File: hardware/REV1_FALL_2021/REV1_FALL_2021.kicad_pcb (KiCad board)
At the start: 2 copper layers, 146 x 133.4 mm, 24 parts, among them J101 Screw_Terminal_01x02, Q101 Q_NMOS_GDS, U1 Teensy3.6_All_Pins, U2 PA16165_Breakout, U201 TPS2113ADRBR, U3 MPL3115A2_Breakout, U301 TPS2113ADRBR, U4 BNO055_Breakout, U5 RFM69HCW_Breakout

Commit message: finish layout
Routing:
- net /BALANCE_CONTROL: track 0.00 -> 55.8 mm, vias 0 -> 1
- net GND: track 157.8 -> 213.3 mm, vias 6 -> 23
- net /TPS_1_STAT: track 3.41 -> 54.9 mm, vias 0 -> 1
- net /TPS_2_STAT: track 4.27 -> 50.5 mm, vias 0 -> 1
- net /V_TEENSY: track 113.5 -> 117.8 mm
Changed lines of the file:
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@@
     (thickness 1.6)
     (drawings 5)
-    (tracks 213)
+    (tracks 275)
     (zones 0)
     (modules 24)
@@
   )
   (setup
-    (last_trace_width 0.762)
+    (last_trace_width 0.25)
     (user_trace_width 0.4318)
     (user_trace_width 0.762)
@@
   (segment (start 104.832998 116.274002) (end 104.832998 120.211002) (width 0.25) (layer B.Cu) (net 11))
   (segment (start 104.832998 116.274002) (end 108.331 112.776) (width 0.25) (layer B.Cu) (net 11))
+  (segment (start 38.0365 88.35) (end 37.126 88.35) (width 0.25) (layer F.Cu) (net 12) (status 400000))
+  (via (at 54.864 89.408) (size 1.016) (drill 0.635) (layers F.Cu B.Cu) (net 12))
+  (segment (start 52.832 91.44) (end 54.864 89.408) (width 0.25) (layer F.Cu) (net 12))
+  (via (at 52.832 91.44) (size 1.016) (drill 0.635) (layers F.Cu B.Cu) (net 12))
+  (segment (start 49.784 91.44) (end 52.832 91.44) (width 0.25) (layer B.Cu) (net 12))
+  (via (at 49.784 91.44) (size 1.016) (drill 0.635) (layers F.Cu B.Cu) (net 12))
+  (segment (start 43.18 91.44) (end 49.784 91.44) (width 0.25) (layer F.Cu) (net 12))
+  (via (at 43.18 91.44) (size 1.016) (drill 0.635) (layers F.Cu B.Cu) (net 12))
+  (segment (start 40.132 91.44) (end 43.18 91.44) (width 0.25) (layer B.Cu) (net 12))
+  (via (at 40.132 91.44) (size 1.016) (drill 0.635) (layers F.Cu B.Cu) (net 12))
+  (segment (start 37.084 91.44) (end 40.132 91.44) (width 0.25) (layer F.Cu) (net 12))
+  (via (at 37.084 91.44) (size 1.016) (drill 0.635) (layers F.Cu B.Cu) (net 12))
+  (segment (start 34.036 91.44) (end 37.084 91.44) (width 0.25) (layer B.Cu) (net 12))
+  (via (at 34.036 91.44) (size 1.016) (drill 0.635) (layers F.Cu B.Cu) (net 12))
+  (segment (start 37.126 88.35) (end 34.036 91.44) (width 0.25) (layer F.Cu) (net 12))
+  (segment (start 42.7765 82.9975) (end 41.4625 82.9975) (width 0.25) (layer F.Cu) (net 12) (status 400000))
+  (via (at 39.624 78.74) (size 1.016) (drill 0.635) (layers F.Cu B.Cu) (net 12))
+  (segment (start 39.624 80.772) (end 39.624 78.74) (width 0.25) (layer F.Cu) (net 12))
+  (segment (start 40.132 81.28) (end 39.624 80.772) (width 0.25) (layer F.Cu) (net 12))
+  (via (at 40.132 81.28) (size 1.016) (drill 0.635) (layers F.Cu B.Cu) (net 12))
+  (segment (start 40.132 84.328) (end 40.132 81.28) (width 0.25) (layer B.Cu) (net 12))
+  (via (at 40.132 84.328) (size 1.016) (drill 0.635) (layers F.Cu B.Cu) (net 12))
+  (segment (start 41.4625 82.9975) (end 40.132 84.328) (width 0.25) (layer F.Cu) (net 12))
+  (segment (start 44.0765 80.1975) (end 44.0765 79.3675) (width 0.25) (layer F.Cu) (net 12) (status 400000))
+  (via (at 53.848 84.836) (size 1.016) (drill 0.635) (layers F.Cu B.Cu) (net 12))
+  (segment (start 54.864 84.836) (end 53.848 84.836) (width 0.25) (layer B.Cu) (net 12))
+  (segment (start 55.88 83.82) (end 54.864 84.836) (width 0.25) (layer B.Cu) (net 12))
+  (via (at 55.88 83.82) (size 1.016) (drill 0.635) (layers F.Cu B.Cu) (net 12))
+  (segment (start 55.88 80.264) (end 55.88 83.82) (width 0.25) (layer F.Cu) (net 12))
+  (segment (start 44.0765 79.3675) (end 44.704 78.74) (width 0.25) (layer F.Cu) (net 12))
+  (segment (start 44.704 78.74) (end 45.212 78.74) (width 0.25) (layer F.Cu) (net 12))
+  (via (at 45.212 78.74) (size 1.016) (drill 0.635) (layers F.Cu B.Cu) (net 12))
+  (segment (start 45.212 78.74) (end 48.26 78.74) (width 0.25) (layer B.Cu) (net 12))
+  (via (at 48.26 78.74) (size 1.016) (drill 0.635) (layers F.Cu B.Cu) (net 12))
+  (segment (start 48.26 78.74) (end 51.308 78.74) (width 0.25) (layer F.Cu) (net 12))
+  (via (at 51.308 78.74) (size 1.016) (drill 0.635) (layers F.Cu B.Cu) (net 12))
+  (segment (start 51.308 78.74) (end 54.356 78.74) (width 0.25) (layer B.Cu) (net 12))
+  (via (at 54.356 78.74) (size 1.016) (drill 0.635) (layers F.Cu B.Cu) (net 12))
+  (segment (start 54.356 78.74) (end 55.88 80.264) (width 0.25) (layer F.Cu) (net 12))
+  (via (at 55.88 80.264) (size 1.016) (drill 0.635) (layers F.Cu B.Cu) (net 12))
   (segment (start 41.473 98.555) (end 41.473 101.854) (width 0.4318) (layer F.Cu) (net 13) (status 400000))
   (segment (start 41.473 101.854) (end 41.473 102.1575) (width 0.4318) (layer F.Cu) (net 13) (status 800000))
@@
   (via (at 46.6725 88.0745) (size 0.8) (drill 0.4) (layers F.Cu B.Cu) (net 14))
   (segment (start 44.873 86.275) (end 46.6725 88.0745) (width 0.4318) (layer F.Cu) (net 14) (status 400000))
-  (segment (start 88.265 157.099) (end 70.739 157.099) (width 0.762) (layer B.Cu) (net 14) (status 400000))
-  (segment (start 60.071 98.425) (end 49.7205 88.0745) (width 0.762) (layer B.Cu) (net 14))
-  (segment (start 60.071 146.431) (end 60.071 98.425) (width 0.762) (layer B.Cu) (net 14))
-  (segment (start 70.739 157.099) (end 60.071 146.431) (width 0.762) (layer B.Cu) (net 14))
+  (segment (start 88.265 157.099) (end 65.659 157.099) (width 0.4318) (layer B.Cu) (net 14) (status 400000))
+  (segment (start 46.6725 92.6465) (end 46.6725 88.0745) (width 0.4318) (layer B.Cu) (net 14))
+  (segment (start 56.769 102.743) (end 46.6725 92.6465) (width 0.4318) (layer B.Cu) (net 14))
+  (segment (start 56.769 148.209) (end 56.769 102.743) (width 0.4318) (layer B.Cu) (net 14))
+  (segment (start 65.659 157.099) (end 56.769 148.209) (width 0.4318) (layer B.Cu) (net 14))
   (segment (start 51.308 118.872) (end 46.99 118.872) (width 0.762) (layer F.Cu) (net 15) (status 400000))
   (segment (start 46.99 118.872) (end 41.529 113.411) (width 0.762) (layer F.Cu) (net 15) (status 800000))
@@
   (segment (start 42.123 95.755) (end 45.828 95.755) (width 0.4318) (layer F.Cu) (net 20) (status C00000))
   (segment (start 45.828 95.755) (end 46.228 96.155) (width 0.4318) (layer F.Cu) (net 20) (status C00000))
+  (segment (start 46.228 96.155) (end 54.975 96.155) (width 0.4318) (layer F.Cu) (net 20) (status 400000))
+  (segment (start 78.105 96.139) (end 88.265 106.299) (width 0.4318) (layer B.Cu) (net 20) (status 800000))
+  (segment (start 63.754 96.139) (end 78.105 96.139) (width 0.4318) (layer B.Cu) (net 20))
+  (segment (start 54.991 96.139) (end 63.754 96.139) (width 0.4318) (layer B.Cu) (net 20))
+  (via (at 54.991 96.139) (size 1.016) (drill 0.635) (layers F.Cu B.Cu) (net 20))
+  (segment (start 54.975 96.155) (end 54.991 96.139) (width 0.4318) (layer F.Cu) (net 20))
   (segment (start 42.7765 80.1975) (end 42.0975 80.1975) (width 0.4318) (layer F.Cu) (net 21) (status 400000))
   (segment (start 41.2115 79.3115) (end 41.2115 76.8825) (width 0.4318) (layer F.Cu) (net 21) (status 800000))
@@
   (segment (start 44.7265 80.1975) (end 45.7965 80.1975) (width 0.4318) (layer F.Cu) (net 22) (status 400000))
   (segment (start 45.7965 80.1975) (end 47.4505 81.8515) (width 0.4318) (layer F.Cu) (net 22) (status 800000))
+  (segment (start 88.265 103.759) (end 66.421 81.915) (width 0.4318) (layer B.Cu) (net 22) (status 400000))
+  (segment (start 49.419 79.883) (end 47.4505 81.8515) (width 0.4318) (layer F.Cu) (net 22) (status 800000))
+  (segment (start 52.578 79.883) (end 49.419 79.883) (width 0.4318) (layer F.Cu) (net 22))
+  (segment (start 52.959 80.264) (end 52.578 79.883) (width 0.4318) (layer F.Cu) (net 22))
+  (via (at 52.959 80.264) (size 1.016) (drill 0.635) (layers F.Cu B.Cu) (net 22))
+  (segment (start 54.61 81.915) (end 52.959 80.264) (width 0.4318) (layer B.Cu) (net 22))
+  (segment (start 66.421 81.915) (end 54.61 81.915) (width 0.4318) (layer B.Cu) (net 22))
+  (segment (start 40.823 95.755) (end 40.823 94.432) (width 0.4318) (layer F.Cu) (net 39) (status 400000))
+  (segment (start 80.772 101.346) (end 88.265 108.839) (width 0.4318) (layer B.Cu) (net 39) (status 800000))
+  (segment (start 61.087 101.346) (end 80.772 101.346) (width 0.4318) (layer B.Cu) (net 39))
+  (segment (start 58.166 101.346) (end 61.087 101.346) (width 0.4318) (layer B.Cu) (net 39))
+  (segment (start 49.911 93.091) (end 58.166 101.346) (width 0.4318) (layer B.Cu) (net 39))
+  (via (at 49.911 93.091) (size 1.016) (drill 0.635) (layers F.Cu B.Cu) (net 39))
+  (segment (start 42.164 93.091) (end 49.911 93.091) (width 0.4318) (layer F.Cu) (net 39))
+  (segment (start 40.823 94.432) (end 42.164 93.091) (width 0.4318) (layer F.Cu) (net 39))
   (segment (start 44.7265 82.9975) (end 44.7265 83.7155) (width 0.4318) (layer F.Cu) (net 113) (status 400000))
   (segment (start 47.286 86.275) (end 49.4665 86.275) (width 0.4318) (layer F.Cu) (net 113) (status 800000))

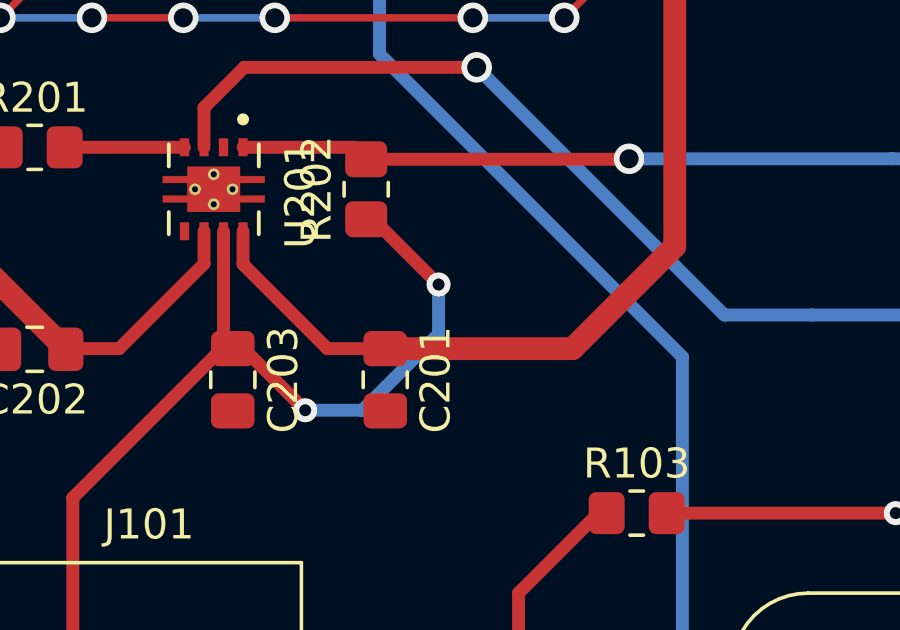
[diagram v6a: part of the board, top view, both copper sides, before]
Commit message: add vias
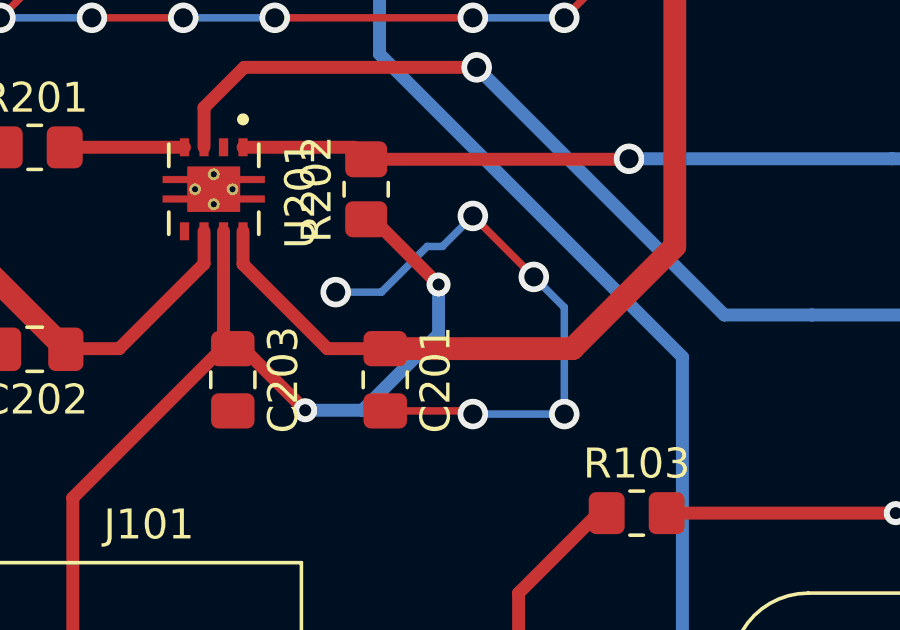
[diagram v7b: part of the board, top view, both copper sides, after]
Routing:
- net GND: track 213.3 -> 232.8 mm, vias 23 -> 28
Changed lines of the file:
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@@
     (thickness 1.6)
     (drawings 5)
-    (tracks 275)
+    (tracks 290)
     (zones 0)
     (modules 24)
@@
   (segment (start 54.356 78.74) (end 55.88 80.264) (width 0.25) (layer F.Cu) (net 12))
   (via (at 55.88 80.264) (size 1.016) (drill 0.635) (layers F.Cu B.Cu) (net 12))
+  (segment (start 46.863 104.5425) (end 49.6785 104.5425) (width 0.25) (layer F.Cu) (net 12) (status 400000))
+  (via (at 45.212 100.584) (size 1.016) (drill 0.635) (layers F.Cu B.Cu) (net 12))
+  (segment (start 46.736 100.584) (end 45.212 100.584) (width 0.25) (layer B.Cu) (net 12))
+  (segment (start 48.26 99.06) (end 46.736 100.584) (width 0.25) (layer B.Cu) (net 12))
+  (segment (start 48.768 99.06) (end 48.26 99.06) (width 0.25) (layer B.Cu) (net 12))
+  (segment (start 49.784 98.044) (end 48.768 99.06) (width 0.25) (layer B.Cu) (net 12))
+  (via (at 49.784 98.044) (size 1.016) (drill 0.635) (layers F.Cu B.Cu) (net 12))
+  (segment (start 51.816 100.076) (end 49.784 98.044) (width 0.25) (layer F.Cu) (net 12))
+  (via (at 51.816 100.076) (size 1.016) (drill 0.635) (layers F.Cu B.Cu) (net 12))
+  (segment (start 52.832 101.092) (end 51.816 100.076) (width 0.25) (layer B.Cu) (net 12))
+  (segment (start 52.832 104.648) (end 52.832 101.092) (width 0.25) (layer B.Cu) (net 12))
+  (segment (start 49.6785 104.5425) (end 49.784 104.648) (width 0.25) (layer F.Cu) (net 12))
+  (via (at 49.784 104.648) (size 1.016) (drill 0.635) (layers F.Cu B.Cu) (net 12))
+  (segment (start 49.784 104.648) (end 52.832 104.648) (width 0.25) (layer B.Cu) (net 12))
+  (via (at 52.832 104.648) (size 1.016) (drill 0.635) (layers F.Cu B.Cu) (net 12))
   (segment (start 41.473 98.555) (end 41.473 101.854) (width 0.4318) (layer F.Cu) (net 13) (status 400000))
   (segment (start 41.473 101.854) (end 41.473 102.1575) (width 0.4318) (layer F.Cu) (net 13) (status 800000))
